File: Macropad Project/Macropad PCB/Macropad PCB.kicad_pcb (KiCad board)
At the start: 2 copper layers, 43 x 63.8 mm, 7 parts, among them SW1 SW_Push, SW2 SW_Push, SW3 SW_Push, SW4 SW_Push, U1 XIAO-RP2040-DIP

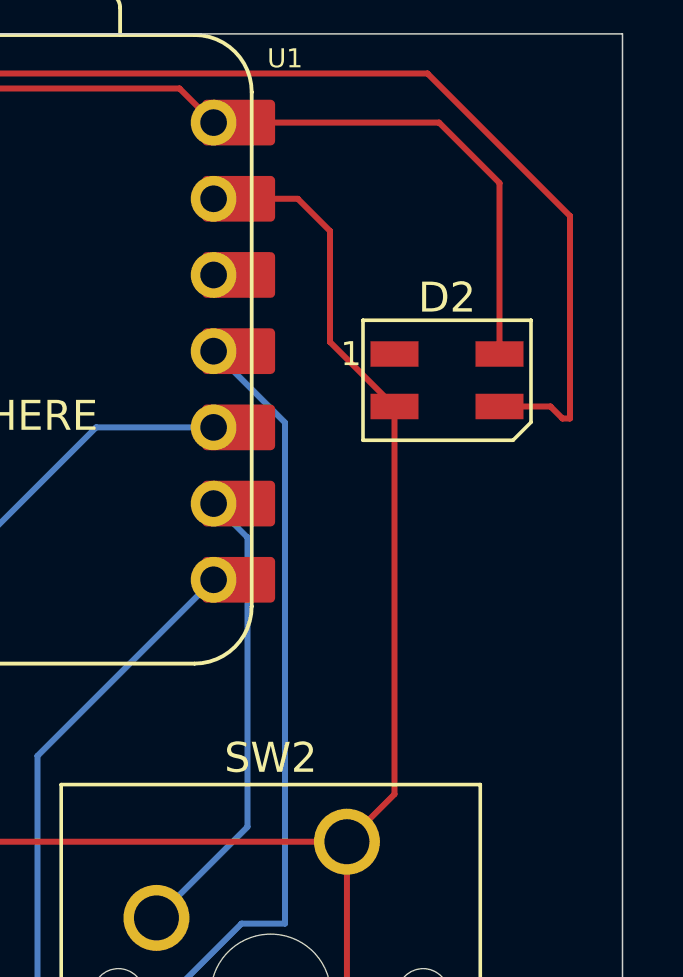
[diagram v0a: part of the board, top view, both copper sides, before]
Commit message: lined up led's
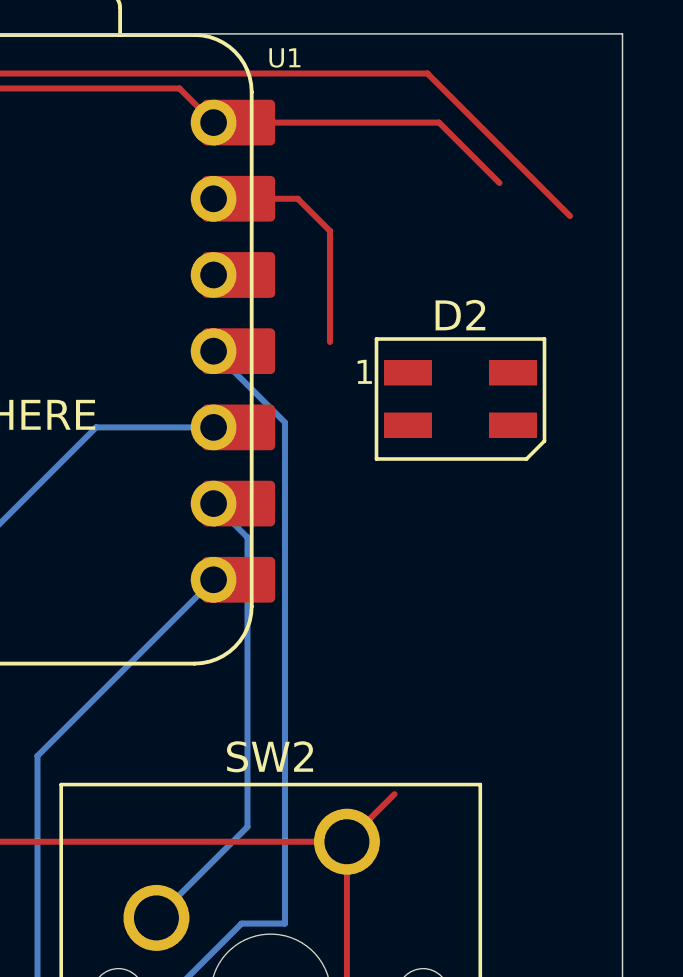
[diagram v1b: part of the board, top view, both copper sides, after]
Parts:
- moved D2 0.77 mm to (111.1, 51.6)
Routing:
- net GND: track 101.9 -> 85.9 mm
- net Net-(D1-DOUT): track 54.9 -> 45.7 mm
- net +5V: track 45.8 -> 40.1 mm
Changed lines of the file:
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@@
 		(allow_soldermask_bridges_in_footprints no)
 		(tenting front back)
+		(grid_origin 116.5 39.45)
 		(pcbplotparams
 			(layerselection 0x00000000_00000000_55555555_5755f5ff)
@@
 	(footprint "LED_SMD:LED_SK6812MINI_PLCC4_3.5x3.5mm_P1.75mm"
 		(layer "F.Cu")
-		(at 110.65 50.975)
+		(at 111.1 51.6)
 		(descr "3.5mm x 3.5mm PLCC4 Addressable RGB LED NeoPixel, https://cdn-shop.adafruit.com/product-files/2686/SK6812MINI_REV.01-1-2.pdf")
 		(tags "LED RGB NeoPixel Mini PLCC-4 3535")
@@
 	)
 	(segment
-		(start 112.4 50.1)
-		(end 112.4 44.4)
-		(width 0.2)
-		(layer "F.Cu")
-		(net 1)
-	)
-	(segment
 		(start 112.4 44.4)
 		(end 110.38625 42.38625)
@@
 	)
 	(segment
-		(start 108.9 51.85)
-		(end 108.9 64.7725)
-		(width 0.2)
-		(layer "F.Cu")
-		(net 2)
-	)
-	(segment
 		(start 105.67625 44.92625)
 		(end 102.87 44.92625)
@@
 	)
 	(segment
-		(start 108.9 51.85)
-		(end 106.75 49.7)
-		(width 0.2)
-		(layer "F.Cu")
-		(net 2)
-	)
-	(segment
 		(start 88.265 66.3575)
 		(end 88.265 85.4075)
@@
 		(layer "F.Cu")
 		(net 2)
-	)
-	(segment
-		(start 114.1 51.85)
-		(end 112.4 51.85)
-		(width 0.2)
-		(layer "F.Cu")
-		(net 3)
-	)
-	(segment
-		(start 114.75 52.25)
-		(end 114.5 52.25)
-		(width 0.2)
-		(layer "F.Cu")
-		(net 3)
 	)
 	(segment
@@
 	)
 	(segment
-		(start 114.5 52.25)
-		(end 114.1 51.85)
-		(width 0.2)
-		(layer "F.Cu")
-		(net 3)
-	)
-	(segment
 		(start 77.15 50.725)
 		(end 77.15 47.35)
 		(width 0.2)
 		(layer "F.Cu")
-		(net 3)
-	)
-	(segment
-		(start 114.75 45.5)
-		(end 114.75 52.25)
-		(width 0.2)
-		(layer "F.Cu")

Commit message: updated README added more keys
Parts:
- added SW5: SW_Push, Button_Switch_Keyboard:SW_Cherry_MX_1.00u_PCB, F.Cu at (88.3, 104.5)
- added SW6: SW_Push, Button_Switch_Keyboard:SW_Cherry_MX_1.00u_PCB, F.Cu at (107.3, 104.5)
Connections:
- U1 pad 6: unconnected-(U1-GPIO7/SCL-Pad6) -> Net-(U1-GPIO7/SCL)
- U1 pad 7: unconnected-(U1-GPIO0/TX-Pad7) -> Net-(U1-GPIO0/TX)
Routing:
- net Net-(U1-GPIO0/TX): track 0.00 -> 62.7 mm, vias 0 -> 1
- net Net-(U1-GPIO7/SCL): track 0.00 -> 57.4 mm, vias 0 -> 1
- net GND: track 85.9 -> 140.3 mm
- net Net-(D1-DOUT): track 45.7 -> 53.5 mm
- net +5V: track 40.1 -> 46.6 mm
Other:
- board size 43 x 63.8 mm -> 43 x 83.2 mm
